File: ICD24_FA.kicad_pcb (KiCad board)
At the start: 2 copper layers, 201.5 x 218 mm, 446 parts, among them J1 Conn_01x02, Q342 2N3904, Q343 2N3904, Q344 2N3904, Q345 2N3904, Q346 2N3904, Q347 2N3904, Q348 2N3904, Q349 2N3904, Q350 2N3904, Q351 2N3904, Q352 2N3904, Q353 2N3904, Q354 2N3904, Q355 2N3904, Q356 2N3904, Q357 2N3904, Q358 2N3904, Q359 2N3904, Q360 2N3904, Q361 2N3904, Q362 2N3904, Q363 2N3904, Q364 2N3904, Q365 2N3904, Q366 2N3904, Q367 2N3904, Q368 2N3904, Q369 2N3904, Q370 2N3904, Q371 2N3904, Q372 2N3904, Q373 2N3904, Q374 2N3904, Q375 2N3904, Q376 2N3904, Q377 2N3904, Q378 2N3904, Q379 2N3904, Q380 2N3904, Q381 2N3904, Q382 2N3904, Q383 2N3904, Q384 2N3904, Q385 2N3904, Q386 2N3904, Q387 2N3904, Q388 2N3904, Q389 2N3904, Q390 2N3904, Q391 2N3904, Q392 2N3904, Q393 2N3904, Q394 2N3904, Q395 2N3904, Q396 2N3904, Q397 2N3904, Q398 2N3904, Q399 2N3904, Q400 2N3904, Q401 2N3904, Q402 2N3904, Q403 2N3904, Q404 2N3904, Q405 2N3904, Q406 2N3904, Q407 2N3904, Q408 2N3904, Q409 2N3904, Q410 2N3904, Q411 2N3904, Q412 2N3904, Q413 2N3904, Q414 2N3904, Q415 2N3904, Q416 2N3904, Q417 2N3904, Q418 2N3904, Q419 2N3904, Q420 2N3904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

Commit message: FA 2-bit
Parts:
- removed D1, D10, D11, D12, D13, D14, D15, D16, D17, D18, D19, D2, D20, D21, D22, D23, D24, D25, D26, D3, D4, D5, D6, D7, D8, D9: LED, LED_THT:LED_D5.0mm
- removed J1: Conn_01x02, Connector_PinHeader_2.54mm:PinHeader_1x02_P2.54mm_Vertical
- removed Q342, Q343, Q344, Q345, Q346, Q347, Q348, Q349, Q350, Q351, Q352, Q353, Q354, Q355, Q356, Q357, Q358, Q359, Q360, Q361, Q362, Q363, Q364, Q365, Q366, Q367, Q368, Q369, Q370, Q371, Q372, Q373, Q374, Q375, Q376, Q377, Q378, Q379, Q380, Q381, Q382, Q383, Q384, Q385, Q386, Q387, Q388, Q389, Q390, Q391, Q392, Q393, Q394, Q395, Q396, Q397, Q398, Q399, Q400, Q401, Q402, Q403, Q404, Q405, Q406, Q407, Q408, Q409, Q410, Q411, Q412, Q413, Q414, Q415, Q416, Q417, Q418, Q419, Q420, Q421, Q422, Q423, Q424, Q425, Q426, Q427, Q428, Q429, Q430, Q431, Q432, Q433, Q434, Q435, Q436, Q437, Q438, Q439, Q440, Q441, Q442, Q443, Q444, Q445, Q446, Q447, Q448, Q449, Q450, Q451, Q452, Q453, Q454, Q455, Q456, Q457, Q458, Q459, Q460, Q461, Q462, Q463, Q464, Q465, Q466, Q467, Q468, Q469, Q470, Q471, Q472, Q473, Q474, Q475, Q476, Q477, Q478, Q479, Q480, Q481, Q482, Q483, Q484, Q485, Q486, Q487, Q488, Q489, Q490, Q491, Q492, Q493: 2N3904, Package_TO_SOT_THT:TO-92_Inline
- removed R530, R531, R532, R534, R535, R536, R537, R538, R539, R540, R542, R543, R544, R545, R546, R547, R548, R550, R551, R552, R554, R555, R556, R558, R559, R560, R562, R563, R564, R565, R566, R567, R568, R570, R571, R572, R573, R574, R575, R576, R578, R579, R580, R582, R583, R584, R586, R587, R588, R590, R591, R592, R593, R594, R595, R596, R598, R599, R600, R601, R602, R603, R604, R606, R607, R608, R610, R611, R612, R614, R615, R616, R618, R619, R620, R621, R622, R623, R624, R626, R627, R628, R629, R630, R631, R632, R634, R635, R636, R638, R639, R640, R642, R643, R644, R646, R647, R648, R649, R650, R651, R652, R654, R655, R656, R657, R658, R659, R660, R662, R663, R664, R666, R667, R668, R670, R671, R672, R674, R675, R676, R677, R678, R679, R680, R682, R683, R684, R685, R686, R687, R688, R690, R691, R692, R694, R695, R696, R698, R699, R700, R702, R703, R704, R705, R706, R707, R708, R710, R711, R712, R713, R714, R715, R716, R718, R719, R720, R722, R723, R724, R726, R727, R728, R730, R731, R732, R733, R734, R735, R736, R738, R739, R740, R741, R742, R743, R744, R746, R747, R748, R750, R751, R752: 220k, Resistor_THT:R_Axial_DIN0309_L9.0mm_D3.2mm_P15.24mm_Horizontal
- removed R533, R541, R549, R553, R557, R561, R569, R57, R577, R58, R581, R585, R589, R59, R597, R60, R605, R609, R61, R613, R617, R62, R625, R63, R633, R637, R64, R641, R645, R65, R653, R66, R661, R665, R669, R67, R673, R68, R681, R689, R69, R693, R697, R70, R701, R709, R71, R717, R72, R721, R725, R729, R73, R737, R74, R745, R749, R75, R753, R754, R76, R77, R78, R79, R80, R81: 47k, Resistor_THT:R_Axial_DIN0309_L9.0mm_D3.2mm_P15.24mm_Horizontal
- removed SW1, SW10, SW11, SW12, SW13, SW14, SW15, SW16, SW17, SW2, SW3, SW4, SW5, SW6, SW7, SW8, SW9: SW_SPDT, MyLibrary:SW_SS12D07VG4
- added D105: LED, LED_THT:LED_D5.0mm, F.Cu at (170.7, 220.2)
- added D106: LED, LED_THT:LED_D5.0mm, F.Cu at (122.5, 220.2)
- added D81: LED, LED_THT:LED_D5.0mm, F.Cu at (163.7, 220.2)
- added D82: LED, LED_THT:LED_D5.0mm, F.Cu at (150.0, 220.2)
- added D83: LED, LED_THT:LED_D5.0mm, F.Cu at (136.2, 220.2)
- added D84: LED, LED_THT:LED_D5.0mm, F.Cu at (157.0, 220.2)
- added D85: LED, LED_THT:LED_D5.0mm, F.Cu at (143.0, 220.2)
- added D86: LED, LED_THT:LED_D5.0mm, F.Cu at (129.2, 220.2)
- added J81: Conn_01x02, Connector_PinHeader_2.54mm:PinHeader_1x02_P2.54mm_Vertical, F.Cu at (136.0, 230.2)
- added Q1: 2N3904, MyLibrary:TO-92_Inline, F.Cu at (144.2, 154.5)
- added Q10: 2N3904, MyLibrary:TO-92_Inline, F.Cu at (124.4, 157.2)
- added Q11: 2N3904, MyLibrary:TO-92_Inline, F.Cu at (109.2, 145.7)
- added Q12: 2N3904, MyLibrary:TO-92_Inline, F.Cu at (125.2, 163.6)
- added Q13: 2N3904, MyLibrary:TO-92_Inline, F.Cu at (109.4, 138.2)
- added Q14: 2N3904, MyLibrary:TO-92_Inline, F.Cu at (119.2, 138.1)
- added Q15: 2N3904, MyLibrary:TO-92_Inline, F.Cu at (103.4, 161.9)
- added Q16: 2N3904, MyLibrary:TO-92_Inline, F.Cu at (104.2, 168.2)
- added Q17: 2N3904, MyLibrary:TO-92_Inline, F.Cu at (119.2, 187.2)
- added Q18: 2N3904, MyLibrary:TO-92_Inline, F.Cu at (109.4, 187.4)
- added Q19: 2N3904, MyLibrary:TO-92_Inline, F.Cu at (119.4, 179.7)
- added Q2: 2N3904, MyLibrary:TO-92_Inline, F.Cu at (143.9, 122.7)
- added Q3: 2N3904, MyLibrary:TO-92_Inline, F.Cu at (135.8, 130.0)
- added Q4: 2N3904, MyLibrary:TO-92_Inline, F.Cu at (137.8, 123.0)
- added Q5: 2N3904, MyLibrary:TO-92_Inline, F.Cu at (138.1, 163.2)
- added Q574: 2N3904, MyLibrary:TO-92_Inline, F.Cu at (206.3, 128.5)
- added Q575: 2N3904, MyLibrary:TO-92_Inline, F.Cu at (208.3, 121.5)
- added Q576: 2N3904, MyLibrary:TO-92_Inline, F.Cu at (214.5, 121.2)
- added Q577: 2N3904, MyLibrary:TO-92_Inline, F.Cu at (174.0, 160.4)
- added Q578: 2N3904, MyLibrary:TO-92_Inline, F.Cu at (174.7, 166.7)
- added Q579: 2N3904, MyLibrary:TO-92_Inline, F.Cu at (180.0, 185.9)
- added Q580: 2N3904, MyLibrary:TO-92_Inline, F.Cu at (190.0, 178.2)
- added Q581: 2N3904, MyLibrary:TO-92_Inline, F.Cu at (189.7, 185.7)
- added Q582: 2N3904, MyLibrary:TO-92_Inline, F.Cu at (195.7, 162.1)
- added Q583: 2N3904, MyLibrary:TO-92_Inline, F.Cu at (195.0, 155.7)
- added Q584: 2N3904, MyLibrary:TO-92_Inline, F.Cu at (189.7, 136.6)
- added Q585: 2N3904, MyLibrary:TO-92_Inline, F.Cu at (179.7, 144.2)
- added Q586: 2N3904, MyLibrary:TO-92_Inline, F.Cu at (180.0, 136.7)
- added Q587: 2N3904, MyLibrary:TO-92_Inline, F.Cu at (208.6, 161.7)
- added Q588: 2N3904, MyLibrary:TO-92_Inline, F.Cu at (215.1, 158.7)
- added Q589: 2N3904, MyLibrary:TO-92_Inline, F.Cu at (214.8, 153.0)
- added Q590: 2N3904, MyLibrary:TO-92_Inline, F.Cu at (226.0, 183.8)
- added Q591: 2N3904, MyLibrary:TO-92_Inline, F.Cu at (219.5, 186.8)
- added Q592: 2N3904, MyLibrary:TO-92_Inline, F.Cu at (219.9, 192.5)
- added Q6: 2N3904, MyLibrary:TO-92_Inline, F.Cu at (144.6, 160.2)
- added Q7: 2N3904, MyLibrary:TO-92_Inline, F.Cu at (155.4, 185.3)
- added Q8: 2N3904, MyLibrary:TO-92_Inline, F.Cu at (149.3, 194.0)
- added Q9: 2N3904, MyLibrary:TO-92_Inline, F.Cu at (148.9, 188.3)
- added R1: 47k, Resistor_THT:R_Axial_DIN0309_L9.0mm_D3.2mm_P15.24mm_Horizontal, F.Cu at (135.8, 150.7)
- added R10: 220k, Resistor_THT:R_Axial_DIN0309_L9.0mm_D3.2mm_P15.24mm_Horizontal, F.Cu at (164.5, 129.0)
- added R11: 47k, Resistor_THT:R_Axial_DIN0309_L9.0mm_D3.2mm_P15.24mm_Horizontal, F.Cu at (126.9, 168.1)
- added R12: 220k, Resistor_THT:R_Axial_DIN0309_L9.0mm_D3.2mm_P15.24mm_Horizontal, F.Cu at (120.9, 160.1)
- added R13: 220k, Resistor_THT:R_Axial_DIN0309_L9.0mm_D3.2mm_P15.24mm_Horizontal, F.Cu at (128.2, 186.7)
- added R137: 47k, Resistor_THT:R_Axial_DIN0309_L9.0mm_D3.2mm_P15.24mm_Horizontal, F.Cu at (165.0, 199.1)
- added R138: 47k, Resistor_THT:R_Axial_DIN0309_L9.0mm_D3.2mm_P15.24mm_Horizontal, F.Cu at (151.5, 199.2)
- added R139: 47k, Resistor_THT:R_Axial_DIN0309_L9.0mm_D3.2mm_P15.24mm_Horizontal, F.Cu at (137.5, 199.0)
- added R14: 220k, Resistor_THT:R_Axial_DIN0309_L9.0mm_D3.2mm_P15.24mm_Horizontal, F.Cu at (128.3, 192.7)
- added R140: 47k, Resistor_THT:R_Axial_DIN0309_L9.0mm_D3.2mm_P15.24mm_Horizontal, F.Cu at (158.0, 199.2)
- added R141: 47k, Resistor_THT:R_Axial_DIN0309_L9.0mm_D3.2mm_P15.24mm_Horizontal, F.Cu at (144.5, 199.2)
- added R142: 47k, Resistor_THT:R_Axial_DIN0309_L9.0mm_D3.2mm_P15.24mm_Horizontal, F.Cu at (130.5, 199.1)
- added R15: 220k, Resistor_THT:R_Axial_DIN0309_L9.0mm_D3.2mm_P15.24mm_Horizontal, F.Cu at (126.4, 136.6)
- added R16: 220k, Resistor_THT:R_Axial_DIN0309_L9.0mm_D3.2mm_P15.24mm_Horizontal, F.Cu at (115.4, 136.1)
- added R161: 47k, Resistor_THT:R_Axial_DIN0309_L9.0mm_D3.2mm_P15.24mm_Horizontal, F.Cu at (172.0, 199.1)
- added R162: 47k, Resistor_THT:R_Axial_DIN0309_L9.0mm_D3.2mm_P15.24mm_Horizontal, F.Cu at (124.0, 199.0)
- added R17: 220k, Resistor_THT:R_Axial_DIN0309_L9.0mm_D3.2mm_P15.24mm_Horizontal, F.Cu at (115.4, 116.6)
- added R18: 220k, Resistor_THT:R_Axial_DIN0309_L9.0mm_D3.2mm_P15.24mm_Horizontal, F.Cu at (120.9, 142.1)
- added R19: 47k, Resistor_THT:R_Axial_DIN0309_L9.0mm_D3.2mm_P15.24mm_Horizontal, F.Cu at (101.7, 157.3)
- added R2: 220k, Resistor_THT:R_Axial_DIN0309_L9.0mm_D3.2mm_P15.24mm_Horizontal, F.Cu at (143.8, 145.7)
- added R20: 220k, Resistor_THT:R_Axial_DIN0309_L9.0mm_D3.2mm_P15.24mm_Horizontal, F.Cu at (109.9, 116.6)
- added R21: 220k, Resistor_THT:R_Axial_DIN0309_L9.0mm_D3.2mm_P15.24mm_Horizontal, F.Cu at (107.7, 165.3)
- added R22: 220k, Resistor_THT:R_Axial_DIN0309_L9.0mm_D3.2mm_P15.24mm_Horizontal, F.Cu at (120.4, 116.6)
- added R23: 220k, Resistor_THT:R_Axial_DIN0309_L9.0mm_D3.2mm_P15.24mm_Horizontal, F.Cu at (102.2, 188.8)
- added R24: 220k, Resistor_THT:R_Axial_DIN0309_L9.0mm_D3.2mm_P15.24mm_Horizontal, F.Cu at (113.2, 189.3)
- added R25: 220k, Resistor_THT:R_Axial_DIN0309_L9.0mm_D3.2mm_P15.24mm_Horizontal, F.Cu at (107.7, 183.3)
- added R26: 220k, Resistor_THT:R_Axial_DIN0309_L9.0mm_D3.2mm_P15.24mm_Horizontal, F.Cu at (108.2, 208.8)
- added R27: 220k, Resistor_THT:R_Axial_DIN0309_L9.0mm_D3.2mm_P15.24mm_Horizontal, F.Cu at (118.7, 208.8)
- added R28: 220k, Resistor_THT:R_Axial_DIN0309_L9.0mm_D3.2mm_P15.24mm_Horizontal, F.Cu at (113.2, 208.8)
- added R3: 220k, Resistor_THT:R_Axial_DIN0309_L9.0mm_D3.2mm_P15.24mm_Horizontal, F.Cu at (165.2, 155.7)
- added R4: 220k, Resistor_THT:R_Axial_DIN0309_L9.0mm_D3.2mm_P15.24mm_Horizontal, F.Cu at (144.6, 181.0)
- added R5: 47k, Resistor_THT:R_Axial_DIN0309_L9.0mm_D3.2mm_P15.24mm_Horizontal, F.Cu at (134.1, 181.0)
- added R6: 220k, Resistor_THT:R_Axial_DIN0309_L9.0mm_D3.2mm_P15.24mm_Horizontal, F.Cu at (148.9, 167.5)
- added R7: 220k, Resistor_THT:R_Axial_DIN0309_L9.0mm_D3.2mm_P15.24mm_Horizontal, F.Cu at (165.3, 161.7)
- added R8: 47k, Resistor_THT:R_Axial_DIN0309_L9.0mm_D3.2mm_P15.24mm_Horizontal, F.Cu at (159.4, 167.5)
- added R835: 220k, Resistor_THT:R_Axial_DIN0309_L9.0mm_D3.2mm_P15.24mm_Horizontal, F.Cu at (214.3, 144.2)
- added R836: 47k, Resistor_THT:R_Axial_DIN0309_L9.0mm_D3.2mm_P15.24mm_Horizontal, F.Cu at (206.3, 149.2)
- added R837: 220k, Resistor_THT:R_Axial_DIN0309_L9.0mm_D3.2mm_P15.24mm_Horizontal, F.Cu at (235.1, 127.5)
- added R838: 220k, Resistor_THT:R_Axial_DIN0309_L9.0mm_D3.2mm_P15.24mm_Horizontal, F.Cu at (235.1, 122.0)
- added R839: 220k, Resistor_THT:R_Axial_DIN0309_L9.0mm_D3.2mm_P15.24mm_Horizontal, F.Cu at (172.7, 187.4)
- added R840: 47k, Resistor_THT:R_Axial_DIN0309_L9.0mm_D3.2mm_P15.24mm_Horizontal, F.Cu at (172.2, 155.9)
- added R841: 220k, Resistor_THT:R_Axial_DIN0309_L9.0mm_D3.2mm_P15.24mm_Horizontal, F.Cu at (178.2, 181.9)
- added R842: 220k, Resistor_THT:R_Axial_DIN0309_L9.0mm_D3.2mm_P15.24mm_Horizontal, F.Cu at (178.2, 163.9)
- added R843: 220k, Resistor_THT:R_Axial_DIN0309_L9.0mm_D3.2mm_P15.24mm_Horizontal, F.Cu at (178.7, 207.4)
- added R844: 220k, Resistor_THT:R_Axial_DIN0309_L9.0mm_D3.2mm_P15.24mm_Horizontal, F.Cu at (183.7, 187.9)
- added R845: 220k, Resistor_THT:R_Axial_DIN0309_L9.0mm_D3.2mm_P15.24mm_Horizontal, F.Cu at (183.7, 207.4)
- added R846: 220k, Resistor_THT:R_Axial_DIN0309_L9.0mm_D3.2mm_P15.24mm_Horizontal, F.Cu at (189.2, 207.4)
- added R847: 220k, Resistor_THT:R_Axial_DIN0309_L9.0mm_D3.2mm_P15.24mm_Horizontal, F.Cu at (197.0, 135.1)
- added R848: 47k, Resistor_THT:R_Axial_DIN0309_L9.0mm_D3.2mm_P15.24mm_Horizontal, F.Cu at (197.5, 166.6)
- added R849: 220k, Resistor_THT:R_Axial_DIN0309_L9.0mm_D3.2mm_P15.24mm_Horizontal, F.Cu at (191.5, 140.6)
- added R850: 220k, Resistor_THT:R_Axial_DIN0309_L9.0mm_D3.2mm_P15.24mm_Horizontal, F.Cu at (191.5, 158.6)
- added R851: 220k, Resistor_THT:R_Axial_DIN0309_L9.0mm_D3.2mm_P15.24mm_Horizontal, F.Cu at (191.0, 115.1)
- added R852: 220k, Resistor_THT:R_Axial_DIN0309_L9.0mm_D3.2mm_P15.24mm_Horizontal, F.Cu at (186.0, 134.6)
- added R853: 220k, Resistor_THT:R_Axial_DIN0309_L9.0mm_D3.2mm_P15.24mm_Horizontal, F.Cu at (186.0, 115.1)
- added R854: 220k, Resistor_THT:R_Axial_DIN0309_L9.0mm_D3.2mm_P15.24mm_Horizontal, F.Cu at (180.5, 115.1)
- added R855: 220k, Resistor_THT:R_Axial_DIN0309_L9.0mm_D3.2mm_P15.24mm_Horizontal, F.Cu at (215.1, 179.5)
- added R856: 47k, Resistor_THT:R_Axial_DIN0309_L9.0mm_D3.2mm_P15.24mm_Horizontal, F.Cu at (204.6, 179.5)
- added R857: 220k, Resistor_THT:R_Axial_DIN0309_L9.0mm_D3.2mm_P15.24mm_Horizontal, F.Cu at (235.9, 160.2)
- added R858: 220k, Resistor_THT:R_Axial_DIN0309_L9.0mm_D3.2mm_P15.24mm_Horizontal, F.Cu at (235.7, 154.2)
- added R859: 220k, Resistor_THT:R_Axial_DIN0309_L9.0mm_D3.2mm_P15.24mm_Horizontal, F.Cu at (219.5, 166.0)
- added R860: 47k, Resistor_THT:R_Axial_DIN0309_L9.0mm_D3.2mm_P15.24mm_Horizontal, F.Cu at (230.0, 166.0)
- added R861: 220k, Resistor_THT:R_Axial_DIN0309_L9.0mm_D3.2mm_P15.24mm_Horizontal, F.Cu at (198.8, 185.2)
- added R862: 220k, Resistor_THT:R_Axial_DIN0309_L9.0mm_D3.2mm_P15.24mm_Horizontal, F.Cu at (198.9, 191.2)
- added R9: 220k, Resistor_THT:R_Axial_DIN0309_L9.0mm_D3.2mm_P15.24mm_Horizontal, F.Cu at (164.5, 123.5)
- added SW81: SW_SPDT, MyLibrary:SW_SS12D07VG4, F.Cu at (165.0, 228.7)
- added SW82: SW_SPDT, MyLibrary:SW_SS12D07VG4, F.Cu at (151.5, 228.7)
- added SW83: SW_SPDT, MyLibrary:SW_SS12D07VG4, F.Cu at (158.0, 228.7)
- added SW84: SW_SPDT, MyLibrary:SW_SS12D07VG4, F.Cu at (144.5, 228.9)
- added SW97: SW_SPDT, MyLibrary:SW_SS12D07VG4, F.Cu at (172.0, 228.7)
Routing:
- net 0: track 0.00 -> 567.2 mm, vias 0 -> 16
- net VDD: track 0.00 -> 511.1 mm, vias 0 -> 20
- net CIN: track 0.00 -> 167.4 mm, vias 0 -> 6
- net IN_B0: track 0.00 -> 144.9 mm, vias 0 -> 4
- net IN_A0: track 0.00 -> 134.6 mm, vias 0 -> 2
- net /fa2_bit/fa1/and_gate/IN_B: track 0.00 -> 114.1 mm
- net /fa2_bit/fa2/and_gate/IN_B: track 0.00 -> 113.8 mm
- net /fa2_bit/fa2/CIN: track 0.00 -> 84.6 mm
- net /fa2_bit/fa2/A: track 0.00 -> 83.4 mm
- net /fa2_bit/fa2/B: track 0.00 -> 73.1 mm
- net /fa2_bit/fa2/and_gate/OUT: track 0.00 -> 61.8 mm
- net /fa2_bit/fa1/and_gate/OUT: track 0.00 -> 61.8 mm
- net /fa2_bit/fa2/and_gate1/OUT: track 0.00 -> 58.8 mm
- net /fa2_bit/fa1/and_gate1/OUT: track 0.00 -> 58.8 mm
- net Net-(Q10-B): track 0.00 -> 52.5 mm, vias 0 -> 2
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- added copper zone on B.Cu, net 0
- added copper zone on F.Cu, net 0
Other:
- board size 201.5 x 218 mm -> 146.5 x 123.5 mm

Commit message: FA8 full sim, before FA1 layout
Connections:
- Q574 pad 3: /fa2_bit/fa2/CARRY_OUT -> OUT_COUT
- Q582 pad 3: /fa2_bit/fa2/SUM -> OUT_SUM1
- R836 pad 2: /fa2_bit/fa2/CARRY_OUT -> OUT_COUT
- R845 pad 1: /fa2_bit/fa2/A -> IN_A1
- R846 pad 1: /fa2_bit/fa2/B -> IN_B1
- R848 pad 2: /fa2_bit/fa2/SUM -> OUT_SUM1
- R854 pad 1: /fa2_bit/fa2/CIN -> /fa2_bit/fa1/CARRY_OUT
- R857 pad 1: /fa2_bit/fa2/A -> IN_A1
- R858 pad 1: /fa2_bit/fa2/B -> IN_B1
- R861 pad 1: /fa2_bit/fa2/CIN -> /fa2_bit/fa1/CARRY_OUT
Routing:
- net /fa2_bit/fa1/CARRY_OUT: track 3.00 -> 139.7 mm
- net IN_B1: track 33.2 -> 156.5 mm, vias 2 -> 4
- net IN_A1: track 33.3 -> 147.9 mm, vias 2 -> 4
- net OUT_COUT: track 0.00 -> 114.2 mm, vias 0 -> 7
- net OUT_SUM1: track 0.00 -> 112.5 mm, vias 0 -> 5
- net /fa2_bit/fa2/CIN: track 84.6 -> 0.00 mm
- net /fa2_bit/fa2/A: track 83.4 -> 0.00 mm
- net /fa2_bit/fa2/B: track 73.1 -> 0.00 mm
- net /fa2_bit/fa2/SUM: track 21.8 -> 0.00 mm
- net /fa2_bit/fa2/CARRY_OUT: track 3.00 -> 0.00 mm

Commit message: FA 1-Bit PCB ok
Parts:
- removed D84, D85, D86: LED, LED_THT:LED_D5.0mm
- removed Q574, Q575, Q576, Q577, Q578, Q579, Q580, Q581, Q582, Q583, Q584, Q585, Q586, Q587, Q588, Q589, Q590, Q591, Q592: 2N3904, MyLibrary:TO-92_Inline
- removed R140, R141, R142, R836, R840, R848, R856, R860: 47k, Resistor_THT:R_Axial_DIN0309_L9.0mm_D3.2mm_P15.24mm_Horizontal
- removed R835, R837, R838, R839, R841, R842, R843, R844, R845, R846, R847, R849, R850, R851, R852, R853, R854, R855, R857, R858, R859, R861, R862: 220k, Resistor_THT:R_Axial_DIN0309_L9.0mm_D3.2mm_P15.24mm_Horizontal
- removed SW83, SW84: SW_SPDT, MyLibrary:SW_SS12D07VG4
- added R20: 220k, MyLibrary:MyPAD, F.Cu at (101.0, 118.0)
- added R20: 220k, MyLibrary:MyPAD, F.Cu at (190.5, 207.7)
- added R20: 220k, MyLibrary:MyPAD, F.Cu at (190.5, 117.5)
- added R20: 220k, MyLibrary:MyPAD, F.Cu at (101.0, 208.2)
- J81: value Conn_01x02 -> Conn_01x08; footprint Connector_PinHeader_2.54mm:PinHeader_1x02_P2.54mm_Vertical -> Connector_PinHeader_2.54mm:PinHeader_1x08_P2.54mm_Horizontal
- moved SW97 96.8 mm to (186.5, 133.0), turned to 180 degrees
- moved SW81 91.3 mm to (186.5, 140.0), turned to 180 degrees
- moved D105 86.3 mm to (178.0, 134.3), turned to 90 degrees
- moved SW82 83.0 mm to (186.5, 153.5), turned to 180 degrees
- moved D81 80.3 mm to (178.0, 141.3), turned to 90 degrees
- moved J81 76.5 mm to (189.6, 175.7), turned to 0 degrees
- moved D82 71.0 mm to (178.0, 155.0), turned to 90 degrees
- moved D106 67.2 mm to (178.0, 182.5), turned to 90 degrees
- moved D83 66.3 mm to (178.0, 168.8), turned to 90 degrees
- moved R161 65.5 mm to (170.0, 133.6), turned to 90 degrees
- moved R162 46.8 mm to (170.0, 207.6), turned to 90 degrees
- moved R137 46.3 mm to (170.0, 153.1), turned to 90 degrees
- moved R139 34.0 mm to (170.0, 189.1), turned to 90 degrees
- moved R138 33.7 mm to (170.0, 171.1), turned to 90 degrees
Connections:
- net /fa2_bit/fa1/and_gate/IN_B renamed /fa1_bit/fa1/and_gate/IN_B
- net /fa2_bit/fa1/and_gate/OUT renamed /fa1_bit/fa1/and_gate/OUT
- net /fa2_bit/fa1/and_gate1/OUT renamed /fa1_bit/fa1/and_gate1/OUT
- J81 pad 2: 0 -> VDD
- Q3 pad 3: /fa2_bit/fa1/CARRY_OUT -> OUT_COUT
- R1 pad 2: /fa2_bit/fa1/CARRY_OUT -> OUT_COUT
- SW97 pad 2: CIN -> CIN_Port
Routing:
- net VDD: track 511.1 -> 281.9 mm, vias 20 -> 12
- net 0: track 567.2 -> 345.7 mm, vias 16 -> 7
- net IN_B1: track 156.5 -> 0.00 mm, vias 4 -> 0
- net IN_A1: track 147.9 -> 0.00 mm, vias 4 -> 0
- net /fa2_bit/fa1/CARRY_OUT: track 139.7 -> 0.00 mm
- net /fa2_bit/fa2/and_gate/IN_B: track 113.8 -> 0.00 mm
- net OUT_SUM1: track 112.5 -> 0.00 mm, vias 5 -> 0
- net CIN: track 167.4 -> 232.7 mm, vias 6 -> 0
- net /fa2_bit/fa2/and_gate/OUT: track 61.8 -> 0.00 mm
- net /fa2_bit/fa2/and_gate1/OUT: track 58.8 -> 0.00 mm
- net CIN_Port: track 0.00 -> 56.0 mm
- net Net-(Q583-B): track 52.5 -> 0.00 mm, vias 2 -> 0
- net Net-(Q578-B): track 43.3 -> 0.00 mm, vias 4 -> 0
- net IN_B0: track 144.9 -> 109.7 mm, vias 4 -> 6
- net OUT_SUM0: track 44.6 -> 77.3 mm
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- removed copper zone on B.Cu, net 0
- removed copper zone on F.Cu, net 0
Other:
- board size 146.5 x 123.5 mm -> 96.3 x 97.5 mm

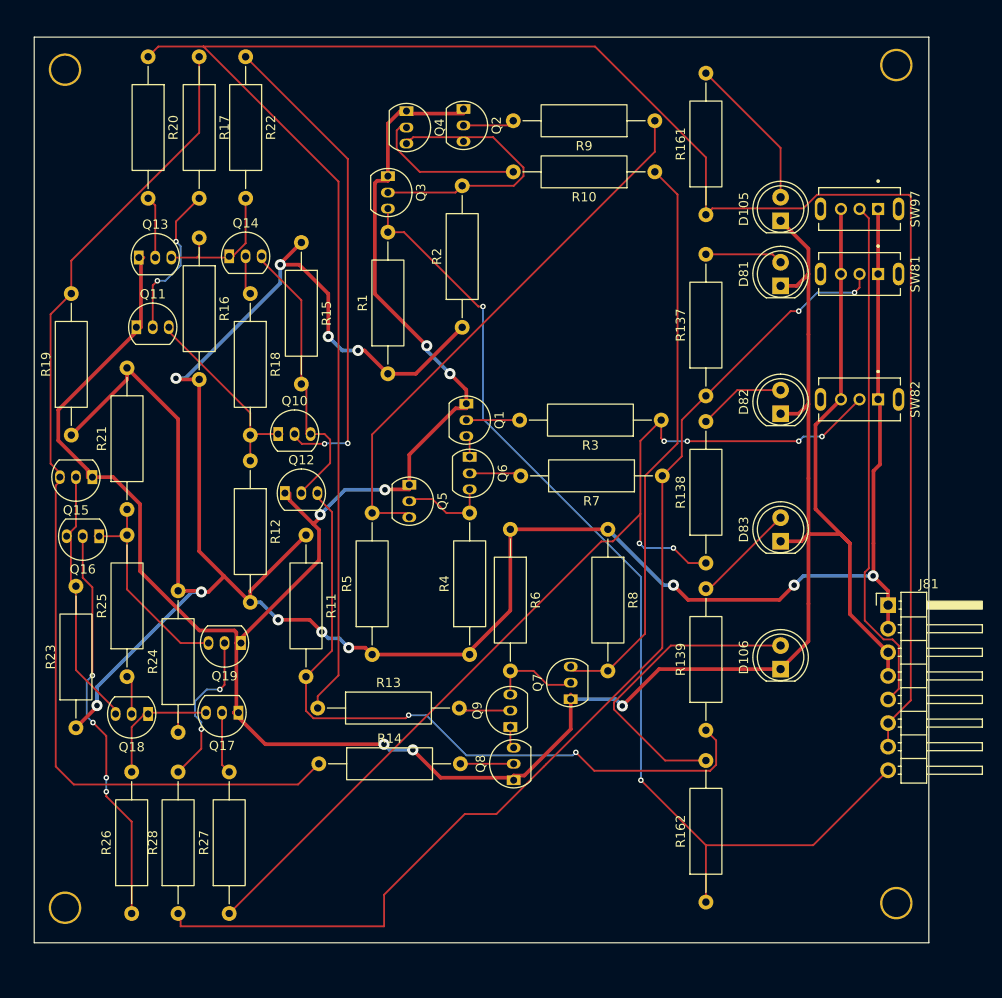
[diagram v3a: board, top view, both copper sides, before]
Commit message: PCB with interconnections
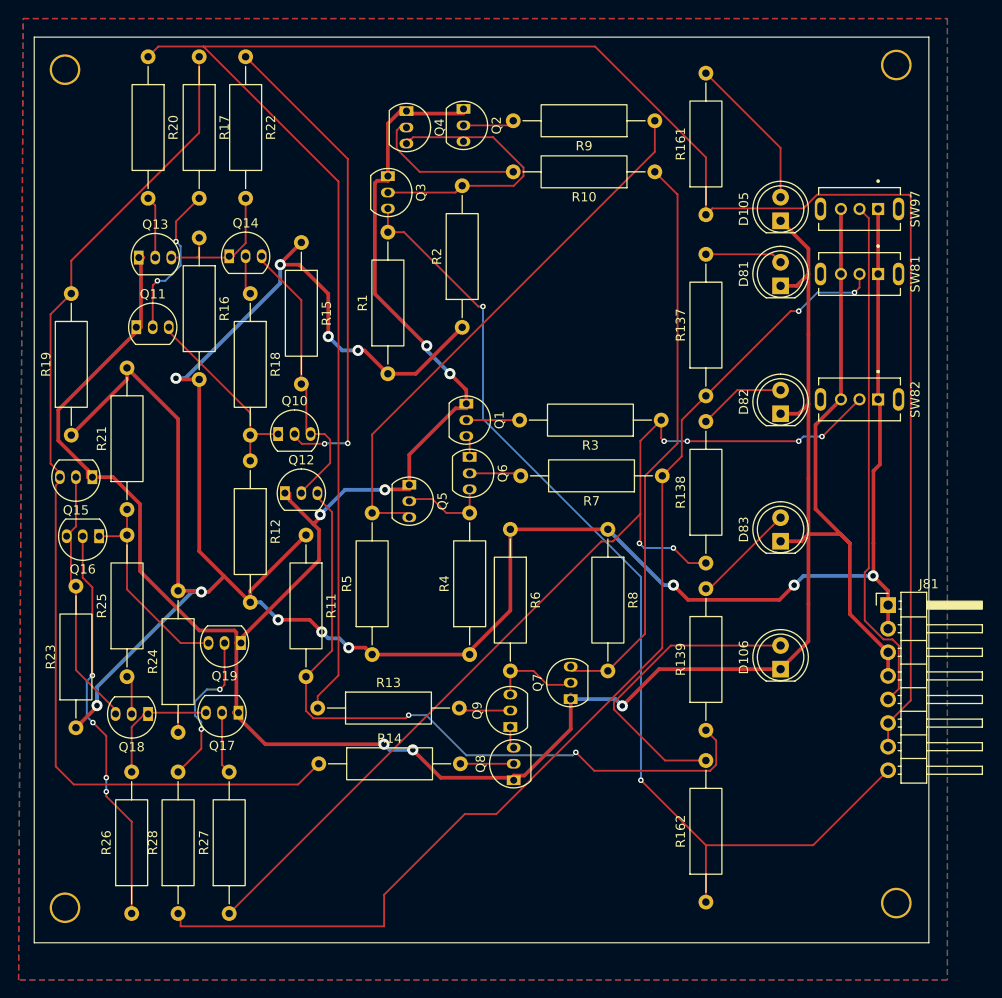
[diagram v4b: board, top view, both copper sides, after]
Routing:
- added copper zone on B.Cu, net 0
- added copper zone on F.Cu, net 0
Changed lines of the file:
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@@
 		(pad "" thru_hole circle
 			(at 0 0 270)
-			(size 3.5 3.5)
-			(drill 3)
+			(size 3.3 3.3)
+			(drill 2.8)
 			(layers "*.Cu" "*.Mask")
 			(remove_unused_layers no)
@@
 		(pad "" thru_hole circle
 			(at 0 0 270)
-			(size 3.5 3.5)
-			(drill 3)
+			(size 3.3 3.3)
+			(drill 2.8)
 			(layers "*.Cu" "*.Mask")
 			(remove_unused_layers no)
@@
 		(pad "" thru_hole circle
 			(at 0 0 270)
-			(size 3.5 3.5)
-			(drill 3)
+			(size 3.3 3.3)
+			(drill 2.8)
 			(layers "*.Cu" "*.Mask")
 			(remove_unused_layers no)
@@
 		(pad "" thru_hole circle
 			(at 0 0 270)
-			(size 3.5 3.5)
-			(drill 3)
+			(size 3.3 3.3)
+			(drill 2.8)
 			(layers "*.Cu" "*.Mask")
 			(remove_unused_layers no)
@@
 		(net 41)
 	)
+	(zone
+		(net 2)
+		(net_name "0")
+		(layers "F.Cu" "B.Cu")
+		(name "GND")
+		(hatch edge 0.5)
+		(connect_pads yes
+			(clearance 0.5)
+		)
+		(min_thickness 0.25)
+		(filled_areas_thickness no)
+		(fill yes
+			(thermal_gap 0.5)
+			(thermal_bridge_width 0.5)
+			(island_removal_mode 1)
+			(island_area_min 10)
+		)
+		(polygon
+			(pts
+				(xy 96.5 112.5) (xy 196 112.5) (xy 196 216) (xy 96 216)
+			)
+		)
+	)
 	(group "and_gate1"

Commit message: BOM and Picture
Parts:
- added G***: LOGO, MyLibrary:DESLabLogo, F.Cu at (144.0, 202.5)
